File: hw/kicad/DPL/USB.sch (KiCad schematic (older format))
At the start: 5 parts, among them J1 USB_B_Micro

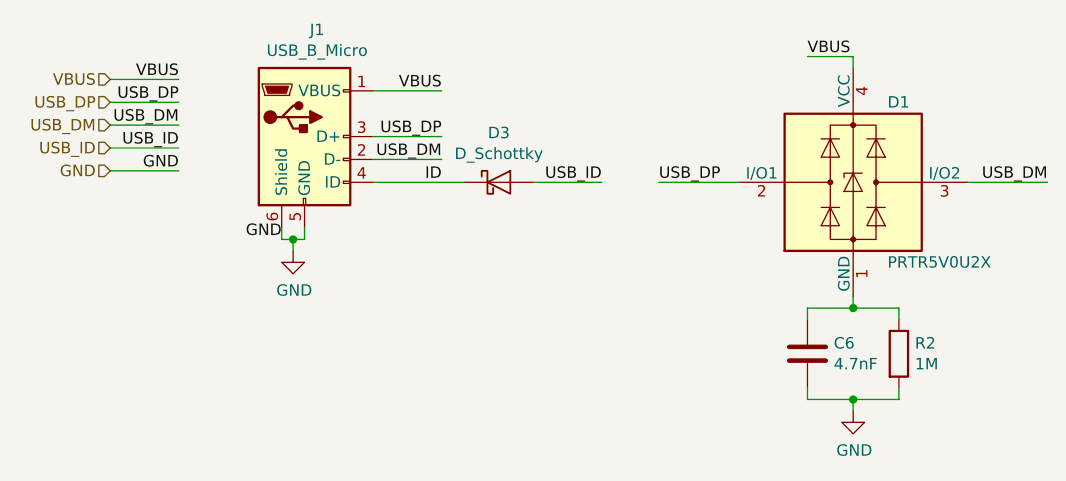
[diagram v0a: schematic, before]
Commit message: Changed the names of some components.
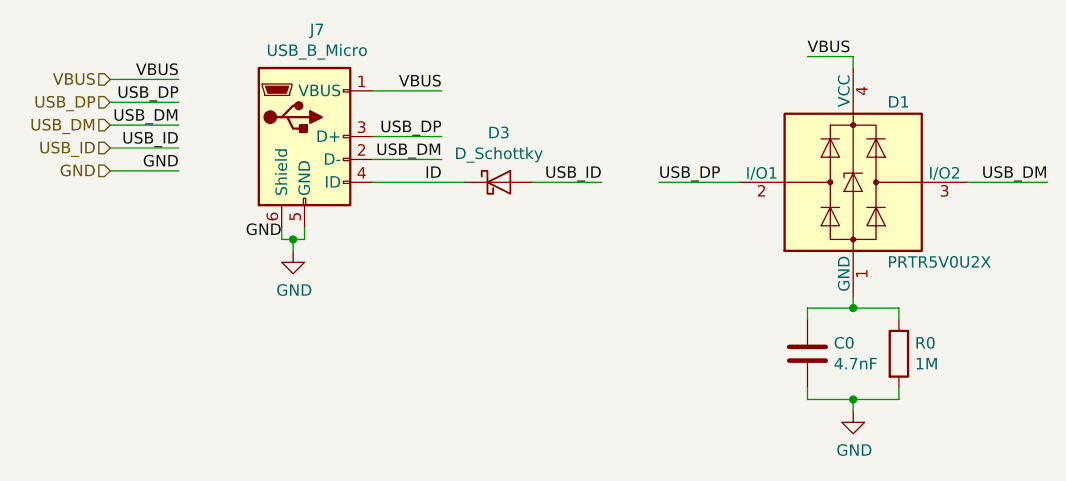
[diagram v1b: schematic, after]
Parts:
- renumbered C6 to C0, J1 to J7, R2 to R0
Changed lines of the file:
@@
 EESchema Schematic File Version 5
+LIBS:DPL-cache
 EELAYER 29 0
 EELAYER END
@@
 $EndDescr
 $Comp
-L Connector:USB_B_Micro J1
+L Connector:USB_B_Micro J7
 U 1 1 5B62635D
 P 5300 3350
-F 0 "J1" H 5355 3817 50  0000 C CNN
+F 0 "J7" H 5355 3817 50  0000 C CNN
 F 1 "USB_B_Micro" H 5355 3726 50  0000 C CNN
 F 2 "Connector_USB:USB_Micro-B_Molex_47346-0001" H 5450 3300 50  0001 C CNN
@@
 $EndComp
 $Comp
-L Device:R R2
+L Device:R R0
 U 1 1 5B62BE0D
 P 7900 4300
-F 0 "R2" H 7970 4346 50  0000 L CNN
+F 0 "R0" H 7970 4346 50  0000 L CNN
 F 1 "1M" H 7970 4255 50  0000 L CNN
 F 2 "Resistor_SMD:R_0603_1608Metric_Pad1.05x0.95mm_HandSolder" V 7830 4300 50  0001 C CNN
@@
 $EndComp
 $Comp
-L Device:C C6
+L Device:C C0
 U 1 1 5B62BE71
 P 7500 4300
-F 0 "C6" H 7615 4346 50  0000 L CNN
+F 0 "C0" H 7615 4346 50  0000 L CNN
 F 1 "4.7nF" H 7615 4255 50  0000 L CNN
 F 2 "Capacitor_SMD:C_0603_1608Metric_Pad1.05x0.95mm_HandSolder" H 7538 4150 50  0001 C CNN

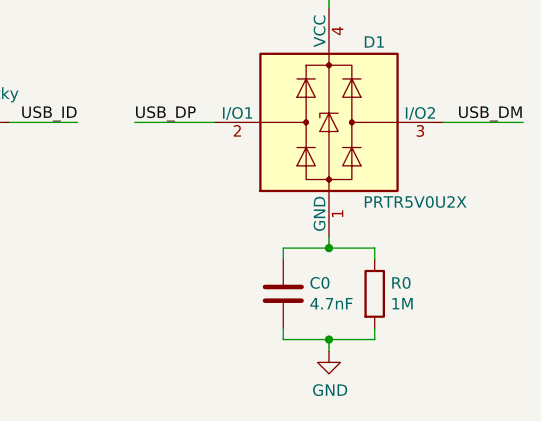
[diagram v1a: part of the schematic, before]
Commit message: Added power selector to the board. Started to design the footprint's layout.
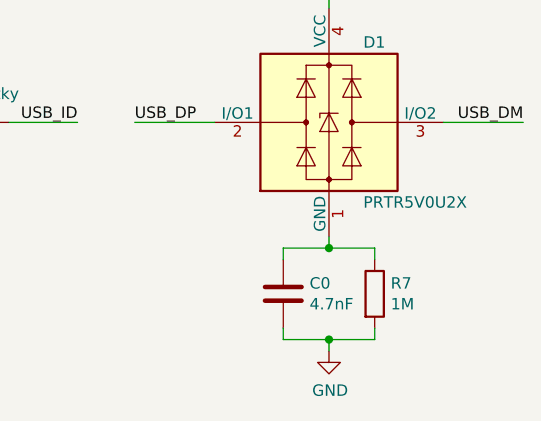
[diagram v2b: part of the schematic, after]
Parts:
- D1: footprint Package_TO_SOT_SMD:SOT-143_Handsoldering -> Package_TO_SOT_SMD:SOT-143
- renumbered R0 to R7
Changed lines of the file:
@@
 F 0 "D1" H 7850 3900 50  0000 L CNN
 F 1 "PRTR5V0U2X" H 7850 3200 50  0000 L CNN
-F 2 "Package_TO_SOT_SMD:SOT-143_Handsoldering" H 7760 3550 50  0001 C CNN
+F 2 "Package_TO_SOT_SMD:SOT-143" H 7760 3550 50  0001 C CNN
 F 3 "https://assets.nexperia.com/documents/data-sheet/PRTR5V0U2X.pdf" H 7760 3550 50  0001 C CNN
 	1    7700 3550
@@
 $EndComp
 $Comp
-L Device:R R0
+L Device:R R7
 U 1 1 5B62BE0D
 P 7900 4300
-F 0 "R0" H 7970 4346 50  0000 L CNN
+F 0 "R7" H 7970 4346 50  0000 L CNN
 F 1 "1M" H 7970 4255 50  0000 L CNN
 F 2 "Resistor_SMD:R_0603_1608Metric_Pad1.05x0.95mm_HandSolder" V 7830 4300 50  0001 C CNN

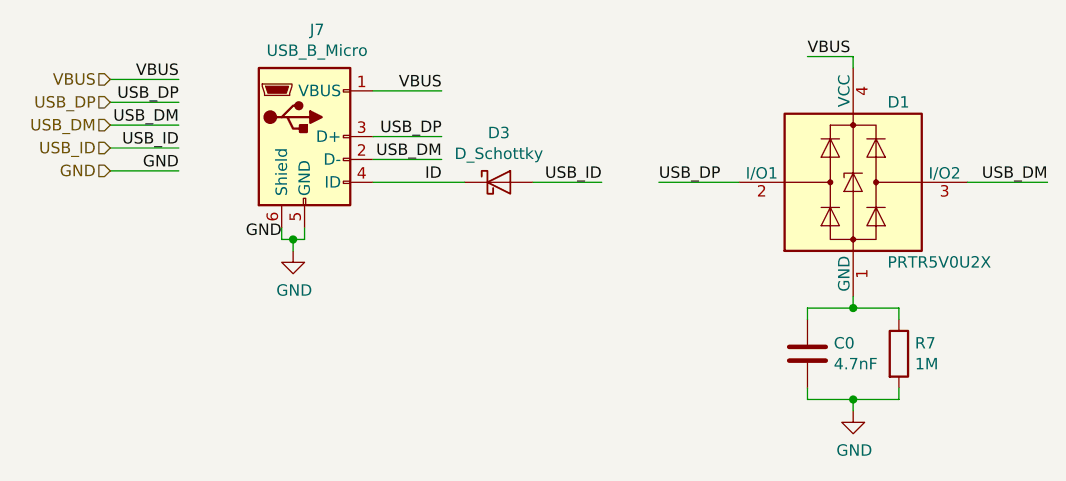
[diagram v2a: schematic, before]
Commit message: Fixed some conections errors. Designed the footprint. Added vias to pass the thread wire of the balloons through them.
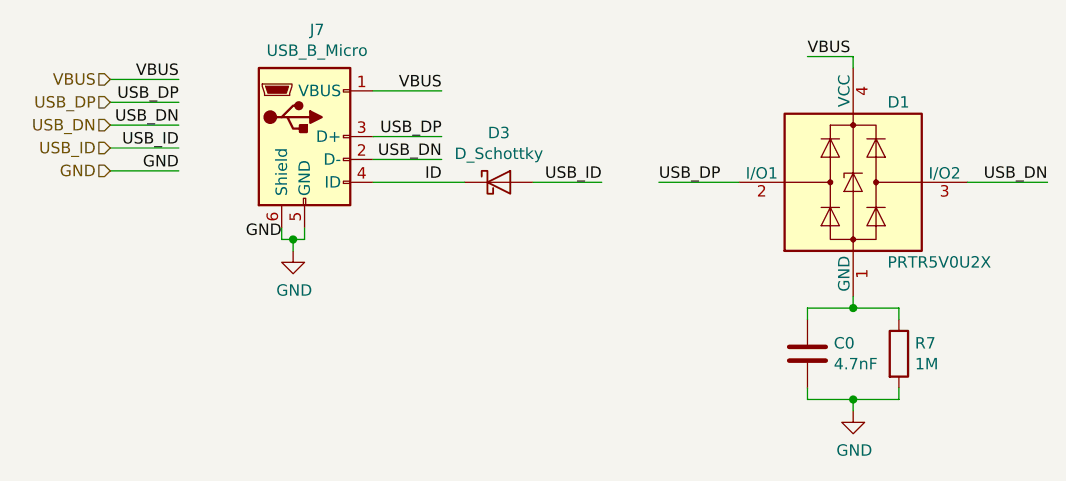
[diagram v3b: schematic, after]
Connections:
- net USB_DM renamed USB_DN
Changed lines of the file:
@@
 USB_DP
 Text Label 5900 3450 2    50   ~ 0
-USB_DM
+USB_DN
 Text Label 6600 3550 2    50   ~ 0
 USB_ID
@@
 	8200 3550 8550 3550
 Text Label 8550 3550 2    50   ~ 0
-USB_DM
+USB_DN
 Wire Wire Line
 	5600 3350 5900 3350
@@
 USB_DP
 Text HLabel 4450 3300 0    50   Input ~ 0
-USB_DM
+USB_DN
 Text HLabel 4450 3400 0    50   Input ~ 0
 USB_ID
@@
 USB_DP
 Text Label 4750 3300 2    50   ~ 0
-USB_DM
+USB_DN
 Text Label 4750 3400 2    50   ~ 0
 USB_ID

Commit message: Improved the USB connection so that the cable doesn't act like an antenna.
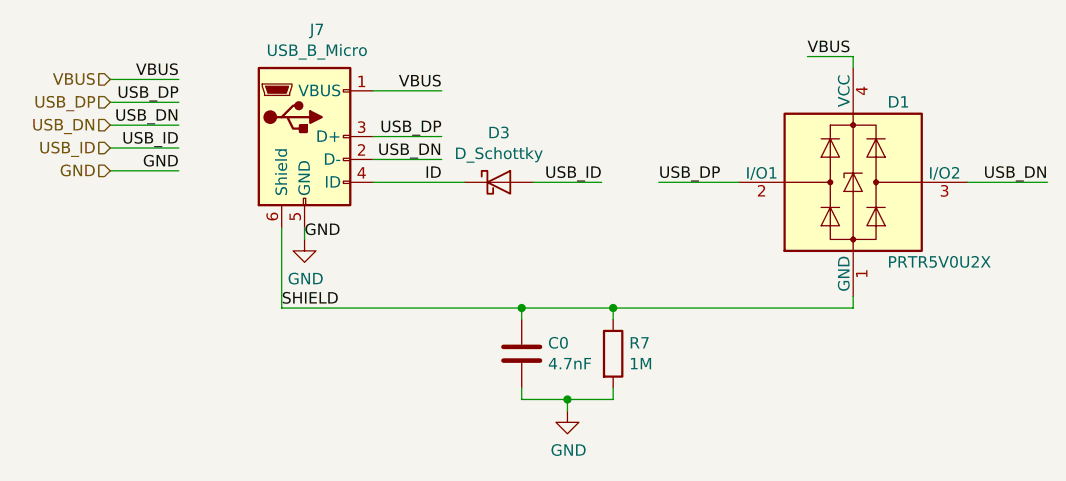
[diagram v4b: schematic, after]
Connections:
- net GND: no longer J7.6 (Shield)
- net SHIELD: now reaches C0.1, D1.1 (GND), R7.1
- net SHIELD: now also J7.6 (Shield)
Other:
- moved on the sheet: C0, R7
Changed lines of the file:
@@
 Text Label 6600 3550 2    50   ~ 0
 USB_ID
-Text Label 5200 3800 2    50   ~ 0
-GND
-Wire Wire Line
-	5200 3750 5200 3800
-Wire Wire Line
-	5200 3800 5250 3800
-Wire Wire Line
-	5300 3800 5300 3750
-Wire Wire Line
-	5250 3800 5250 3850
-Connection ~ 5250 3800
-Wire Wire Line
-	5250 3800 5300 3800
 $Comp
 L power:GND #PWR0102
 U 1 1 5B62BD38
-P 5250 3850
-F 0 "#PWR0102" H 5250 3600 50  0001 C CNN
-F 1 "GND" H 5255 3677 50  0000 C CNN
-F 2 "" H 5250 3850 50  0001 C CNN
-F 3 "" H 5250 3850 50  0001 C CNN
-	1    5250 3850
+P 5300 3800
+F 0 "#PWR0102" H 5300 3550 50  0001 C CNN
+F 1 "GND" H 5305 3627 50  0000 C CNN
+F 2 "" H 5300 3800 50  0001 C CNN
+F 3 "" H 5300 3800 50  0001 C CNN
+	1    5300 3800
 	1    0    0    -1
 $EndComp
@@
 L Device:R R7
 U 1 1 5B62BE0D
-P 7900 4300
-F 0 "R7" H 7970 4346 50  0000 L CNN
-F 1 "1M" H 7970 4255 50  0000 L CNN
-F 2 "Resistor_SMD:R_0603_1608Metric_Pad1.05x0.95mm_HandSolder" V 7830 4300 50  0001 C CNN
-F 3 "~" H 7900 4300 50  0001 C CNN
-	1    7900 4300
+P 6650 4300
+F 0 "R7" H 6720 4346 50  0000 L CNN
+F 1 "1M" H 6720 4255 50  0000 L CNN
+F 2 "Resistor_SMD:R_0603_1608Metric_Pad1.05x0.95mm_HandSolder" V 6580 4300 50  0001 C CNN
+F 3 "~" H 6650 4300 50  0001 C CNN
+	1    6650 4300
 	1    0    0    -1
 $EndComp
@@
 L Device:C C0
 U 1 1 5B62BE71
-P 7500 4300
-F 0 "C0" H 7615 4346 50  0000 L CNN
-F 1 "4.7nF" H 7615 4255 50  0000 L CNN
-F 2 "Capacitor_SMD:C_0603_1608Metric_Pad1.05x0.95mm_HandSolder" H 7538 4150 50  0001 C CNN
-F 3 "~" H 7500 4300 50  0001 C CNN
-	1    7500 4300
+P 6250 4300
+F 0 "C0" H 6365 4346 50  0000 L CNN
+F 1 "4.7nF" H 6365 4255 50  0000 L CNN
+F 2 "Capacitor_SMD:C_0603_1608Metric_Pad1.05x0.95mm_HandSolder" H 6288 4150 50  0001 C CNN
+F 3 "~" H 6250 4300 50  0001 C CNN
+	1    6250 4300
 	1    0    0    -1
 $EndComp
 Wire Wire Line
-	7500 4150 7500 4100
+	6250 4150 6250 4100
 Wire Wire Line
-	7500 4100 7700 4100
-Wire Wire Line
-	7900 4100 7900 4150
+	6650 4100 6650 4150
 Wire Wire Line
 	7700 4050 7700 4100
-Connection ~ 7700 4100
 Wire Wire Line
-	7700 4100 7900 4100
+	6250 4450 6250 4500
 Wire Wire Line
-	7500 4450 7500 4500
+	6250 4500 6450 4500
 Wire Wire Line
-	7500 4500 7700 4500
+	6650 4500 6650 4450
 Wire Wire Line
-	7900 4500 7900 4450
+	6450 4500 6450 4550
+Connection ~ 6450 4500
 Wire Wire Line
-	7700 4500 7700 4550
-Connection ~ 7700 4500
-Wire Wire Line
-	7700 4500 7900 4500
+	6450 4500 6650 4500
 $Comp
 L power:GND #PWR0103
 U 1 1 5BA44753
-P 7700 4550
-F 0 "#PWR0103" H 7700 4300 50  0001 C CNN
-F 1 "GND" H 7705 4377 50  0000 C CNN
-F 2 "" H 7700 4550 50  0001 C CNN
-F 3 "" H 7700 4550 50  0001 C CNN
-	1    7700 4550
+P 6450 4550
+F 0 "#PWR0103" H 6450 4300 50  0001 C CNN
+F 1 "GND" H 6455 4377 50  0000 C CNN
+F 2 "" H 6450 4550 50  0001 C CNN
+F 3 "" H 6450 4550 50  0001 C CNN
+	1    6450 4550
 	1    0    0    -1
 $EndComp
@@
 Wire Wire Line
 	5600 3550 6000 3550
+Wire Wire Line
+	6250 4100 6650 4100
+Wire Wire Line
+	7700 4100 6650 4100
+Connection ~ 6650 4100
+Wire Wire Line
+	6250 4100 5200 4100
+Wire Wire Line
+	5200 3750 5200 4100
+Connection ~ 6250 4100
+Wire Wire Line
+	5300 3750 5300 3800
+Text Label 5200 4100 0    50   ~ 0
+SHIELD
+Text Label 5300 3800 0    50   ~ 0
+GND
 $EndSCHEMATC
